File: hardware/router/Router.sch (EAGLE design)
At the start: 51 parts, among them J0 CON-MATENLOK, J1 AVR_PROG, J10 RJ45-8PTH, J11 RJ45-8PTH, J12 RJ45-8PTH, J13 RJ45-8PTH, J14 RJ45-8PTH, J15 RJ45-8PTH, J16 RJ45-8PTH, J17 RASPBERRYPI_BB, J18 RJ45-8PTH, J19 RJ45-8PTH, J2 RJ45-8PTH, J3 RJ45-8PTH, J4 RJ45-8PTH, J5 RJ45-8PTH, J6 RJ45-8PTH, J7 RJ45-8PTH, J8 RJ45-8PTH, J9 RJ45-8PTH, Q1 NMOS, Q2 NMOS, Q3 NMOS, U1 ATMEGA168, U3 DS1307SO8, Y1 32.768kHz

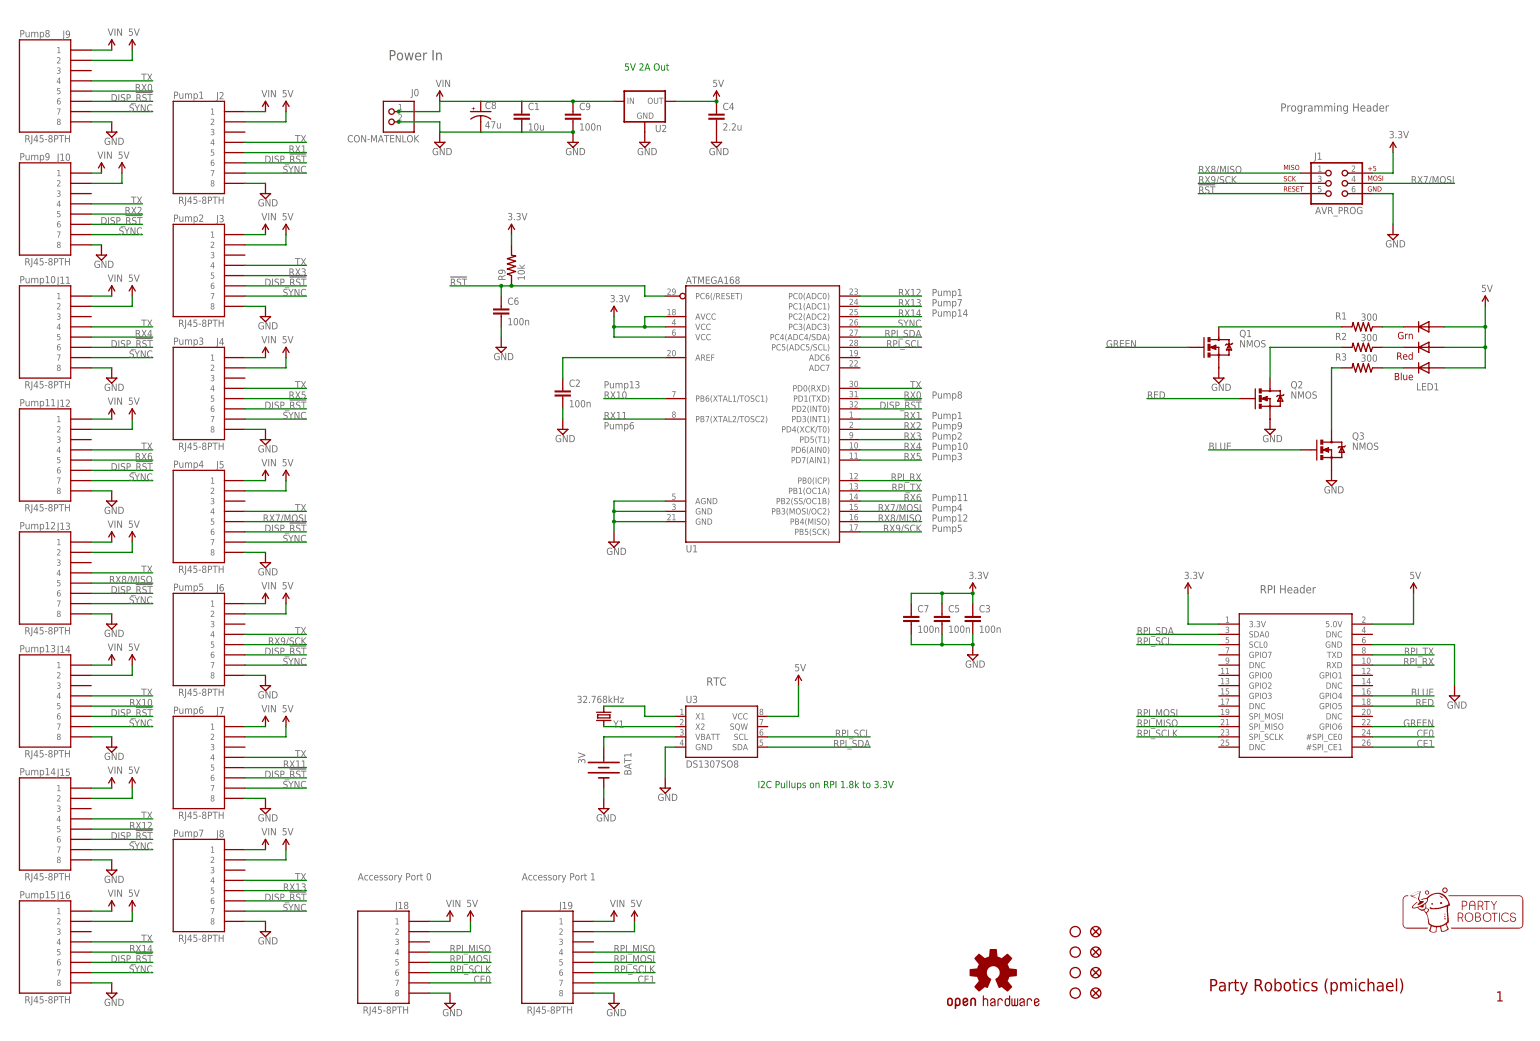
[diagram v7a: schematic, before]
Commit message: Updated to schematic and layout to Rev 1.1 (PD0 and PD1 swapped)
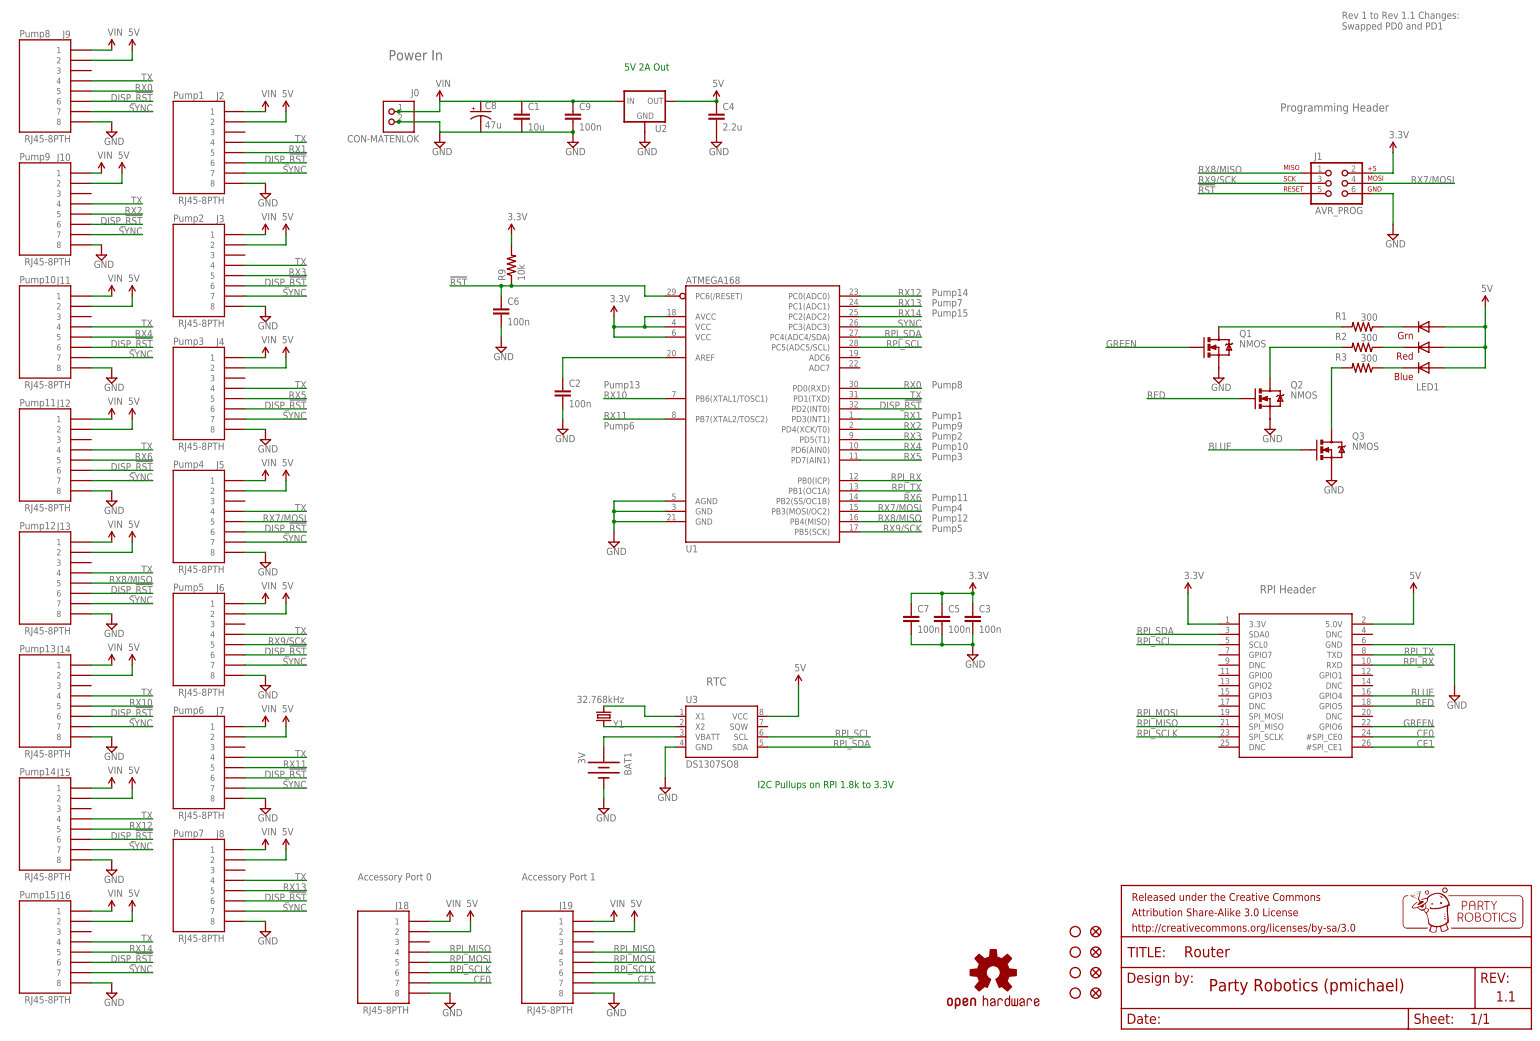
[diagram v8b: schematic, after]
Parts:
- added FRAME3: FRAME-LETTER, SparkFun-Aesthetics:FRAME-LETTER
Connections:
- net RX0: now also U1.PD0(RXD); no longer U1.PD1(TXD)
- net TX: now also U1.PD1(TXD); no longer U1.PD0(RXD)
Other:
- note added: "1.1"
- note added: "Rev 1 to Rev 1.1 Changes: Swapped PD0 and PD1"
- note removed: "1"
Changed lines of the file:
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@@
 <part name="J17" library="pierre" deviceset="RASPBERRYPI_B" device="B"/>
 <part name="U$46" library="SparkFun-Aesthetics" deviceset="OSHW-LOGO" device="M"/>
+<part name="FRAME3" library="SparkFun-Aesthetics" deviceset="FRAME-LETTER" device=""/>
 </parts>
 <sheets>
@@
 <text x="193.04" y="63.5" size="1.778" layer="91">I2C Pullups on RPI 1.8k to 3.3V</text>
 <text x="134.62" y="40.64" size="1.778" layer="95">Accessory Port 1</text>
+<frame x1="0" y1="0" x2="388.62" y2="261.62" columns="8" rows="5" layer="94"/>
+<text x="48.26" y="234.315" size="1.778" layer="95">Pump1</text>
+<text x="48.26" y="203.835" size="1.778" layer="95">Pump2</text>
+<text x="10.16" y="219.075" size="1.778" layer="95">Pump9</text>
+<text x="10.16" y="249.555" size="1.778" layer="95">Pump8</text>
+<text x="10.16" y="188.595" size="1.778" layer="95">Pump10</text>
+<text x="10.16" y="158.115" size="1.778" layer="95">Pump11</text>
+<text x="48.26" y="173.355" size="1.778" layer="95">Pump3</text>
+<text x="48.26" y="142.875" size="1.778" layer="95">Pump4</text>
+<text x="10.16" y="127.635" size="1.778" layer="95">Pump12</text>
+<text x="48.26" y="112.395" size="1.778" layer="95">Pump5</text>
+<text x="10.16" y="97.155" size="1.778" layer="95">Pump13</text>
+<text x="48.26" y="81.915" size="1.778" layer="95">Pump6</text>
+<text x="10.16" y="66.675" size="1.778" layer="95">Pump14</text>
+<text x="48.26" y="51.435" size="1.778" layer="95">Pump7</text>
+<text x="10.16" y="36.195" size="1.778" layer="95">Pump15</text>
+<text x="236.22" y="185.42" size="1.778" layer="95">Pump14</text>
+<text x="236.22" y="182.88" size="1.778" layer="95">Pump7</text>
+<text x="236.22" y="180.34" size="1.778" layer="95">Pump15</text>
+<text x="236.22" y="162.56" size="1.778" layer="95">Pump8</text>
+<text x="236.22" y="154.94" size="1.778" layer="95">Pump1</text>
+<text x="236.22" y="152.4" size="1.778" layer="95">Pump9</text>
+<text x="236.22" y="149.86" size="1.778" layer="95">Pump2</text>
+<text x="236.22" y="147.32" size="1.778" layer="95">Pump10</text>
+<text x="236.22" y="144.78" size="1.778" layer="95">Pump3</text>
+<text x="236.22" y="134.62" size="1.778" layer="95">Pump11</text>
+<text x="236.22" y="132.08" size="1.778" layer="95">Pump4</text>
+<text x="236.22" y="129.54" size="1.778" layer="95">Pump12</text>
+<text x="236.22" y="127" size="1.778" layer="95">Pump5</text>
+<text x="154.94" y="162.56" size="1.778" layer="95">Pump13</text>
+<text x="154.94" y="152.4" size="1.778" layer="95">Pump6</text>
+<text x="337.82" y="251.46" size="1.778" layer="95">Rev 1 to Rev 1.1 Changes:
+Swapped PD0 and PD1</text>
 <text x="304.8508" y="13.1572" size="3.048" layer="94" font="vector" distance="30">Party Robotics (pmichael)</text>
-<frame x1="0" y1="0" x2="388.62" y2="261.62" columns="8" rows="5" layer="94"/>
-<text x="375.9708" y="10.6172" size="2.54" layer="94" font="vector" distance="30">1</text>
+<text x="375.9708" y="10.6172" size="2.54" layer="94" font="vector" distance="30">1.1</text>
 <rectangle x1="360.14025" y1="27.71775" x2="360.96575" y2="27.78125" layer="94"/>
 <rectangle x1="360.01325" y1="27.78125" x2="361.15625" y2="27.84475" layer="94"/>
@@
 <rectangle x1="363.06125" y1="38.76675" x2="363.69625" y2="38.83025" layer="94"/>
 <rectangle x1="363.25175" y1="38.83025" x2="363.50575" y2="38.89375" layer="94"/>
-<text x="48.26" y="234.315" size="1.778" layer="95">Pump1</text>
-<text x="48.26" y="203.835" size="1.778" layer="95">Pump2</text>
-<text x="10.16" y="219.075" size="1.778" layer="95">Pump9</text>
-<text x="10.16" y="249.555" size="1.778" layer="95">Pump8</text>
-<text x="10.16" y="188.595" size="1.778" layer="95">Pump10</text>
-<text x="10.16" y="158.115" size="1.778" layer="95">Pump11</text>
-<text x="48.26" y="173.355" size="1.778" layer="95">Pump3</text>
-<text x="48.26" y="142.875" size="1.778" layer="95">Pump4</text>
-<text x="10.16" y="127.635" size="1.778" layer="95">Pump12</text>
-<text x="48.26" y="112.395" size="1.778" layer="95">Pump5</text>
-<text x="10.16" y="97.155" size="1.778" layer="95">Pump13</text>
-<text x="48.26" y="81.915" size="1.778" layer="95">Pump6</text>
-<text x="10.16" y="66.675" size="1.778" layer="95">Pump14</text>
-<text x="48.26" y="51.435" size="1.778" layer="95">Pump7</text>
-<text x="10.16" y="36.195" size="1.778" layer="95">Pump15</text>
-<text x="236.22" y="185.42" size="1.778" layer="95">Pump1</text>
-<text x="236.22" y="182.88" size="1.778" layer="95">Pump7</text>
-<text x="236.22" y="180.34" size="1.778" layer="95">Pump14</text>
-<text x="236.22" y="160.02" size="1.778" layer="95">Pump8</text>
-<text x="236.22" y="154.94" size="1.778" layer="95">Pump1</text>
-<text x="236.22" y="152.4" size="1.778" layer="95">Pump9</text>
-<text x="236.22" y="149.86" size="1.778" layer="95">Pump2</text>
-<text x="236.22" y="147.32" size="1.778" layer="95">Pump10</text>
-<text x="236.22" y="144.78" size="1.778" layer="95">Pump3</text>
-<text x="236.22" y="134.62" size="1.778" layer="95">Pump11</text>
-<text x="236.22" y="132.08" size="1.778" layer="95">Pump4</text>
-<text x="236.22" y="129.54" size="1.778" layer="95">Pump12</text>
-<text x="236.22" y="127" size="1.778" layer="95">Pump5</text>
-<text x="154.94" y="162.56" size="1.778" layer="95">Pump13</text>
-<text x="154.94" y="152.4" size="1.778" layer="95">Pump6</text>
 </plain>
 <instances>
@@
 <instance part="J17" gate="G$1" x="325.12" y="88.9"/>
 <instance part="U$46" gate="G$1" x="251.46" y="17.78"/>
+<instance part="FRAME3" gate="G$2" x="283.21" y="3.81"/>
 </instances>
 <busses>
@@
 </segment>
 <segment>
-<wire x1="233.68" y1="160.02" x2="218.44" y2="160.02" width="0.1524" layer="91"/>
-<label x="233.68" y="160.02" size="1.778" layer="95" rot="MR0"/>
-<pinref part="U1" gate="G$1" pin="PD1(TXD)"/>
+<wire x1="233.68" y1="162.56" x2="218.44" y2="162.56" width="0.1524" layer="91"/>
+<label x="233.68" y="162.56" size="1.778" layer="95" rot="MR0"/>
+<pinref part="U1" gate="G$1" pin="PD0(RXD)"/>
 </segment>
 </net>
@@
 <net name="TX" class="0">
 <segment>
-<wire x1="233.68" y1="162.56" x2="218.44" y2="162.56" width="0.1524" layer="91"/>
-<label x="233.68" y="162.56" size="1.778" layer="95" rot="MR0"/>
-<pinref part="U1" gate="G$1" pin="PD0(RXD)"/>
-</segment>
-<segment>
 <pinref part="J9" gate="G$1" pin="4"/>
 <wire x1="27.94" y1="238.76" x2="43.18" y2="238.76" width="0.1524" layer="91"/>
@@
 <label x="43.18" y="25.4" size="1.778" layer="95" rot="MR0"/>
 <pinref part="J16" gate="G$1" pin="4"/>
+</segment>
+<segment>
+<wire x1="233.68" y1="160.02" x2="218.44" y2="160.02" width="0.1524" layer="91"/>
+<label x="233.68" y="160.02" size="1.778" layer="95" rot="MR0"/>
+<pinref part="U1" gate="G$1" pin="PD1(TXD)"/>
 </segment>
 </net>
@@
 </schematic>
 </drawing>
+<compatibility>
+<note version="6.3" minversion="6.2.2" severity="warning">
+Since Version 6.2.2 text objects can contain more than one line,
+which will not be processed correctly with this version.
+</note>
+</compatibility>
 </eagle>
